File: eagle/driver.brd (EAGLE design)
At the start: 101.6 x 76.2 mm, 89 parts, among them IC1 XMEGA128A1, IC10 ST95P08M, IC11 ST95P08M, IC12 ST95P08M, IC13 ST95P08M, IC14 ST95P08M, IC15 ST95P08M, IC16 74AHC1G02DBV, IC17 74AHC1G02DBV, IC18 74AHC1G125DBV, IC19 74AHC1G125DBV, IC2 74AC16244, IC20 ST95P08M, IC21 ST95P08M, IC22 ST95P08M, IC23 ST95P08M, IC24 ST95P08M, IC25 ST95P08M, IC3 74AC16244, IC4 74AC16244, IC5 74AC16244, IC6 74AC16374, IC7 74AC16374, IC8 74AC16374, IC9 74AC16374

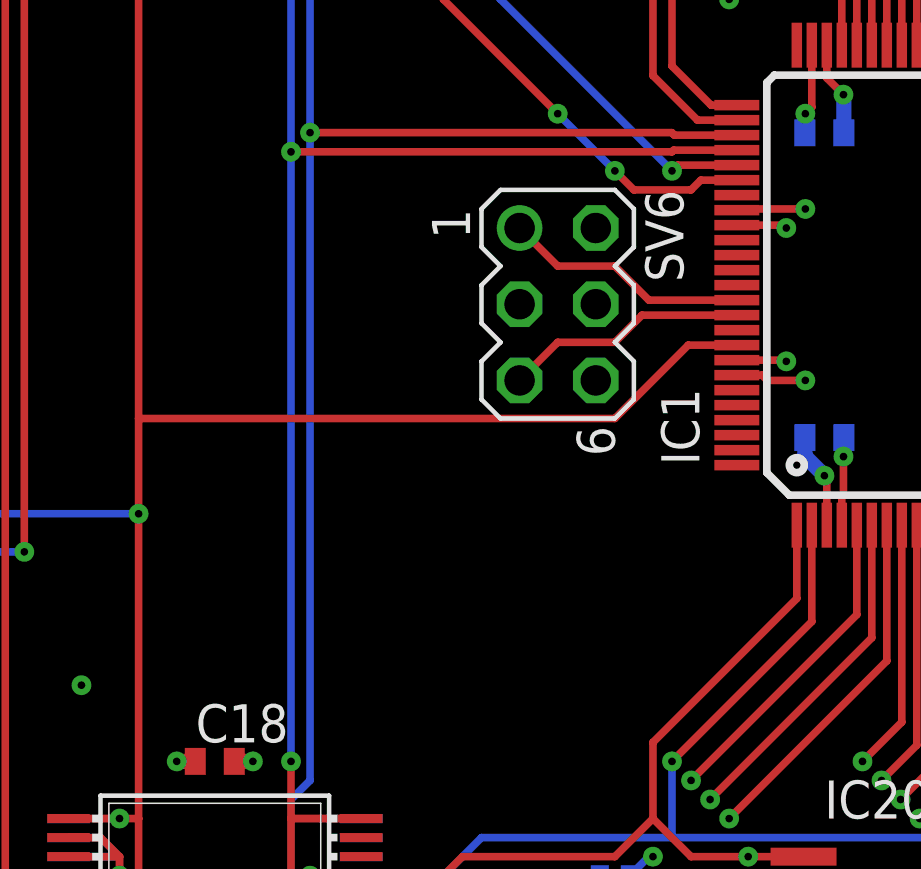
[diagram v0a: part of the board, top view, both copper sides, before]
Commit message: add reset button and status leds
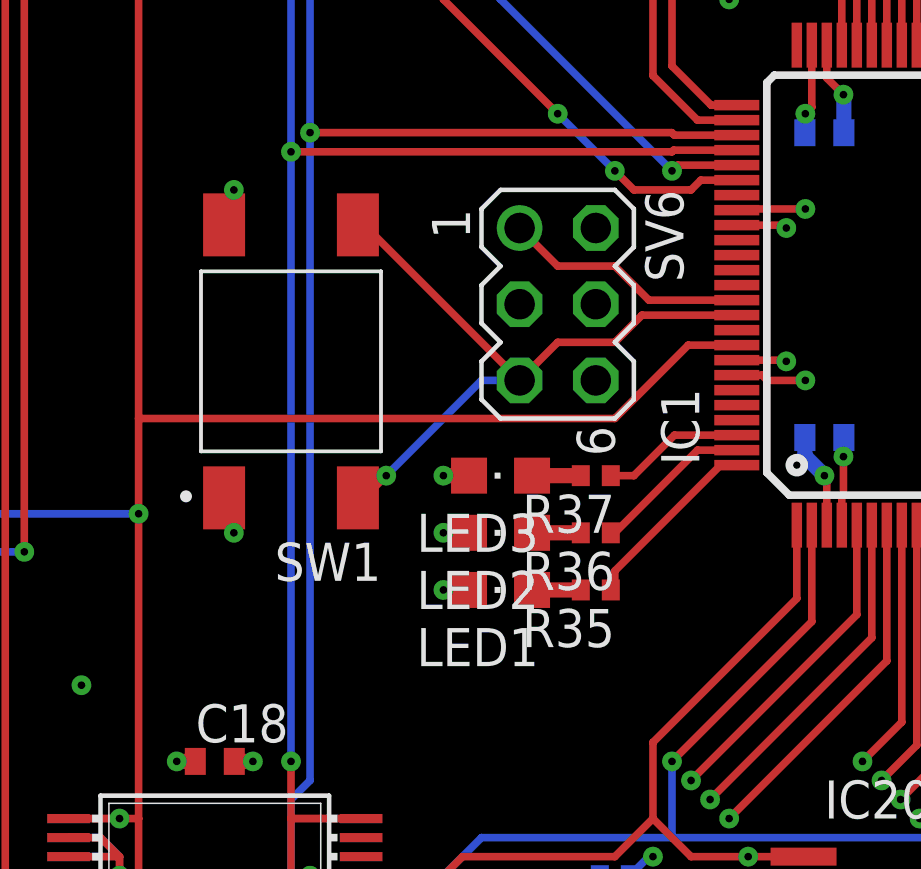
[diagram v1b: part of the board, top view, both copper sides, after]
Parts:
- added LED1, LED2, LED3: (no value), led:CHIPLED_0805
- added R35, R36, R37: 330, rcl:R0402
- added SW1: FSM2JSMA, Switch:FSM2JSMA
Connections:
- removed net N$88: IC1.90, SV6.5
- new net N$63: IC1.90, SV6.5, SW1.3, SW1.4
- new net N$66: LED3.A, R37.2
- new net N$67: LED2.A, R36.2
- new net N$69: LED1.A, R35.2
- new net N$71: IC1.100, R35.1
- new net N$73: IC1.99, R36.1
- new net N$75: IC1.98, R37.1
- net GND: now also LED1.C, LED2.C, LED3.C, SW1.1, SW1.2
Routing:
- net N$63: track 0.00 -> 22.7 mm, vias 0 -> 1
- net N$88: track 8.14 -> 0.00 mm
- net N$71: track 0.00 -> 6.22 mm
- net N$73: track 0.00 -> 5.34 mm
- net GND: track 187.5 -> 192.7 mm, vias 96 -> 101
- net N$75: track 0.00 -> 4.76 mm
- net N$69: track 0.00 -> 1.62 mm
- net N$67: track 0.00 -> 1.62 mm
- net N$66: track 0.00 -> 1.62 mm
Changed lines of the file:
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@@
 <layer number="132" name="bAdjust" color="7" fill="1" visible="yes" active="yes"/>
 <layer number="144" name="Drill_legend" color="7" fill="1" visible="yes" active="yes"/>
+<layer number="145" name="DrillLegend_01-16" color="2" fill="9" visible="no" active="yes"/>
+<layer number="146" name="DrillLegend_01-20" color="3" fill="9" visible="no" active="yes"/>
 <layer number="150" name="Notes" color="7" fill="1" visible="yes" active="yes"/>
 <layer number="151" name="HeatSink" color="7" fill="1" visible="yes" active="yes"/>
@@
 <attribute name="VALUE" x="36.195" y="13.335" size="1.27" layer="28" rot="MR0"/>
 </element>
+<element name="SW1" library="Switch" library_urn="urn:adsk.eagle:library:11396471" package="FSM2JSMA" package3d_urn="urn:adsk.eagle:package:12788212/3" value="FSM2JSMA" x="24.765" y="35.56" smashed="yes" rot="R180">
+<attribute name="CREATED_BY" value="PCBLayout.com" x="24.765" y="35.56" size="1.778" layer="27" rot="R180" display="off"/>
+<attribute name="DIGIKEY_PART_NUMBER" value="450-1130-ND" x="24.765" y="35.56" size="1.778" layer="27" rot="R180" display="off"/>
+<attribute name="MANUFACTURER" value="TE Connectivity ALCOSWITCH Switches" x="24.765" y="35.56" size="1.778" layer="27" rot="R180" display="off"/>
+<attribute name="MPN" value="FSM2JSMA" x="24.765" y="35.56" size="1.778" layer="27" rot="R180" display="off"/>
+<attribute name="NAME" x="27.76896875" y="29.51536875" size="1.27168125" layer="25" rot="R180"/>
+<attribute name="VALUE" x="28.01793125" y="42.85428125" size="1.27115" layer="27" rot="R180"/>
+</element>
+<element name="R35" library="rcl" library_urn="urn:adsk.eagle:library:334" package="R0402" package3d_urn="urn:adsk.eagle:package:23547/3" value="330" x="34.925" y="27.94" smashed="yes" rot="R180">
+<attribute name="NAME" x="35.56" y="27.305" size="1.27" layer="25" rot="R180"/>
+<attribute name="POPULARITY" value="34" x="34.925" y="27.94" size="1.778" layer="27" rot="R180" display="off"/>
+<attribute name="SPICEPREFIX" value="R" x="34.925" y="27.94" size="1.778" layer="27" rot="R180" display="off"/>
+<attribute name="VALUE" x="35.56" y="29.845" size="1.27" layer="27" rot="R180"/>
+</element>
+<element name="R36" library="rcl" library_urn="urn:adsk.eagle:library:334" package="R0402" package3d_urn="urn:adsk.eagle:package:23547/3" value="330" x="34.925" y="29.845" smashed="yes" rot="R180">
+<attribute name="NAME" x="35.56" y="29.21" size="1.27" layer="25" rot="R180"/>
+<attribute name="POPULARITY" value="34" x="34.925" y="29.845" size="1.778" layer="27" rot="R180" display="off"/>
+<attribute name="SPICEPREFIX" value="R" x="34.925" y="29.845" size="1.778" layer="27" rot="R180" display="off"/>
+<attribute name="VALUE" x="35.56" y="31.75" size="1.27" layer="27" rot="R180"/>
+</element>
+<element name="R37" library="rcl" library_urn="urn:adsk.eagle:library:334" package="R0402" package3d_urn="urn:adsk.eagle:package:23547/3" value="330" x="34.925" y="31.75" smashed="yes" rot="R180">
+<attribute name="NAME" x="35.56" y="31.115" size="1.27" layer="25" rot="R180"/>
+<attribute name="POPULARITY" value="34" x="34.925" y="31.75" size="1.778" layer="27" rot="R180" display="off"/>
+<attribute name="SPICEPREFIX" value="R" x="34.925" y="31.75" size="1.778" layer="27" rot="R180" display="off"/>
+<attribute name="VALUE" x="35.56" y="33.655" size="1.27" layer="27" rot="R180"/>
+</element>
+<element name="LED1" library="led" library_urn="urn:adsk.eagle:library:259" package="CHIPLED_0805" package3d_urn="urn:adsk.eagle:package:15821/2" value="" x="31.75" y="27.94" smashed="yes" rot="R90">
+<attribute name="NAME" x="33.02" y="26.67" size="1.27" layer="25" rot="R180"/>
+<attribute name="POPULARITY" value="52" x="31.75" y="27.94" size="1.778" layer="27" rot="R90" display="off"/>
+<attribute name="VALUE" x="33.02" y="30.48" size="1.27" layer="27" rot="R180"/>
+</element>
+<element name="LED2" library="led" library_urn="urn:adsk.eagle:library:259" package="CHIPLED_0805" package3d_urn="urn:adsk.eagle:package:15821/2" value="" x="31.75" y="29.845" smashed="yes" rot="R90">
+<attribute name="NAME" x="33.02" y="28.575" size="1.27" layer="25" rot="R180"/>
+<attribute name="POPULARITY" value="52" x="31.75" y="29.845" size="1.778" layer="27" rot="R90" display="off"/>
+<attribute name="VALUE" x="33.02" y="32.385" size="1.27" layer="27" rot="R180"/>
+</element>
+<element name="LED3" library="led" library_urn="urn:adsk.eagle:library:259" package="CHIPLED_0805" package3d_urn="urn:adsk.eagle:package:15821/2" value="" x="31.75" y="31.75" smashed="yes" rot="R90">
+<attribute name="NAME" x="33.02" y="30.48" size="1.27" layer="25" rot="R180"/>
+<attribute name="POPULARITY" value="52" x="31.75" y="31.75" size="1.778" layer="27" rot="R90" display="off"/>
+<attribute name="VALUE" x="33.02" y="34.29" size="1.27" layer="27" rot="R180"/>
+</element>
 </elements>
 <signals>
@@
 <wire x1="17.3482" y1="17.78" x2="18.415" y2="17.78" width="0.254" layer="16"/>
 <wire x1="18.415" y1="17.78" x2="19.05" y2="18.415" width="0.254" layer="16"/>
+<contactref element="SW1" pad="1"/>
+<contactref element="SW1" pad="2"/>
+<via x="22.86" y="41.275" extent="1-16" drill="0.254"/>
+<via x="22.86" y="29.845" extent="1-16" drill="0.254"/>
+<wire x1="22.535" y1="40.11" x2="22.535" y2="40.95" width="0.254" layer="1"/>
+<wire x1="22.535" y1="40.95" x2="22.86" y2="41.275" width="0.254" layer="1"/>
+<wire x1="22.535" y1="31.01" x2="22.86" y2="30.685" width="0.254" layer="1"/>
+<wire x1="22.86" y1="30.685" x2="22.86" y2="29.845" width="0.254" layer="1"/>
+<contactref element="LED1" pad="C"/>
+<contactref element="LED2" pad="C"/>
+<contactref element="LED3" pad="C"/>
+<via x="29.845" y="31.75" extent="1-16" drill="0.254"/>
+<via x="29.845" y="29.845" extent="1-16" drill="0.254"/>
+<via x="29.845" y="27.94" extent="1-16" drill="0.254"/>
+<wire x1="30.7" y1="31.75" x2="29.845" y2="31.75" width="0.508" layer="1"/>
+<wire x1="30.7" y1="29.845" x2="29.845" y2="29.845" width="0.508" layer="1"/>
+<wire x1="30.7" y1="27.94" x2="29.845" y2="27.94" width="0.508" layer="1"/>
 </signal>
 <signal name="VCC">
@@
 <wire x1="33.655" y1="38.735" x2="32.385" y2="40.005" width="0.254" layer="1"/>
 </signal>
-<signal name="N$88">
-<contactref element="IC1" pad="90"/>
-<contactref element="SV6" pad="5"/>
-<wire x1="39.625" y1="37.1" x2="36.465" y2="37.1" width="0.254" layer="1"/>
-<wire x1="36.465" y1="37.1" x2="35.56" y2="36.195" width="0.254" layer="1"/>
-<wire x1="35.56" y1="36.195" x2="33.655" y2="36.195" width="0.254" layer="1"/>
-<wire x1="33.655" y1="36.195" x2="32.385" y2="34.925" width="0.254" layer="1"/>
-</signal>
 <signal name="N$89">
 <contactref element="IC1" pad="38"/>
@@
 <wire x1="48.625" y1="23.765" x2="51.435" y2="20.955" width="0.254" layer="1"/>
 </signal>
+<signal name="N$63">
+<contactref element="SW1" pad="4"/>
+<contactref element="SW1" pad="3"/>
+<contactref element="IC1" pad="90"/>
+<contactref element="SV6" pad="5"/>
+<wire x1="39.625" y1="37.1" x2="36.465" y2="37.1" width="0.254" layer="1"/>
+<wire x1="36.465" y1="37.1" x2="35.56" y2="36.195" width="0.254" layer="1"/>
+<wire x1="35.56" y1="36.195" x2="33.655" y2="36.195" width="0.254" layer="1"/>
+<wire x1="33.655" y1="36.195" x2="32.385" y2="34.925" width="0.254" layer="1"/>
+<wire x1="32.385" y1="34.925" x2="27.2" y2="40.11" width="0.254" layer="1"/>
+<wire x1="27.2" y1="40.11" x2="26.995" y2="40.11" width="0.254" layer="1"/>
+<via x="27.94" y="31.75" extent="1-16" drill="0.254"/>
+<wire x1="27.94" y1="31.75" x2="27.2" y2="31.01" width="0.254" layer="1"/>
+<wire x1="27.2" y1="31.01" x2="26.995" y2="31.01" width="0.254" layer="1"/>
+<wire x1="27.94" y1="31.75" x2="31.115" y2="34.925" width="0.254" layer="16"/>
+<wire x1="31.115" y1="34.925" x2="32.385" y2="34.925" width="0.254" layer="16"/>
+</signal>
+<signal name="N$66">
+<contactref element="R37" pad="2"/>
+<contactref element="LED3" pad="A"/>
+<wire x1="32.8" y1="31.75" x2="34.425" y2="31.75" width="0.508" layer="1"/>
+</signal>
+<signal name="N$67">
+<contactref element="R36" pad="2"/>
+<contactref element="LED2" pad="A"/>
+<wire x1="32.8" y1="29.845" x2="34.425" y2="29.845" width="0.508" layer="1"/>
+</signal>
+<signal name="N$69">
+<contactref element="R35" pad="2"/>
+<contactref element="LED1" pad="A"/>
+<wire x1="32.8" y1="27.94" x2="34.425" y2="27.94" width="0.508" layer="1"/>
+</signal>
+<signal name="N$71">
+<contactref element="IC1" pad="100"/>
+<contactref element="R35" pad="1"/>
+<wire x1="35.425" y1="27.94" x2="35.56" y2="28.075" width="0.254" layer="1"/>
+<wire x1="35.56" y1="28.075" x2="35.56" y2="28.575" width="0.254" layer="1"/>
+<wire x1="39.085" y1="32.1" x2="39.625" y2="32.1" width="0.254" layer="1"/>
+<wire x1="35.56" y1="28.575" x2="39.085" y2="32.1" width="0.254" layer="1"/>
+</signal>
+<signal name="N$73">
+<contactref element="R36" pad="1"/>
+<contactref element="IC1" pad="99"/>
+<wire x1="35.425" y1="29.845" x2="35.56" y2="29.845" width="0.254" layer="1"/>
+<wire x1="38.315" y1="32.6" x2="39.625" y2="32.6" width="0.254" layer="1"/>
+<wire x1="35.56" y1="29.845" x2="38.315" y2="32.6" width="0.254" layer="1"/>
+</signal>
+<signal name="N$75">
+<contactref element="IC1" pad="98"/>
+<contactref element="R37" pad="1"/>
+<wire x1="35.425" y1="31.75" x2="36.195" y2="31.75" width="0.254" layer="1"/>
+<wire x1="37.545" y1="33.1" x2="39.625" y2="33.1" width="0.254" layer="1"/>
+<wire x1="36.195" y1="31.75" x2="37.545" y2="33.1" width="0.254" layer="1"/>
+</signal>
 </signals>

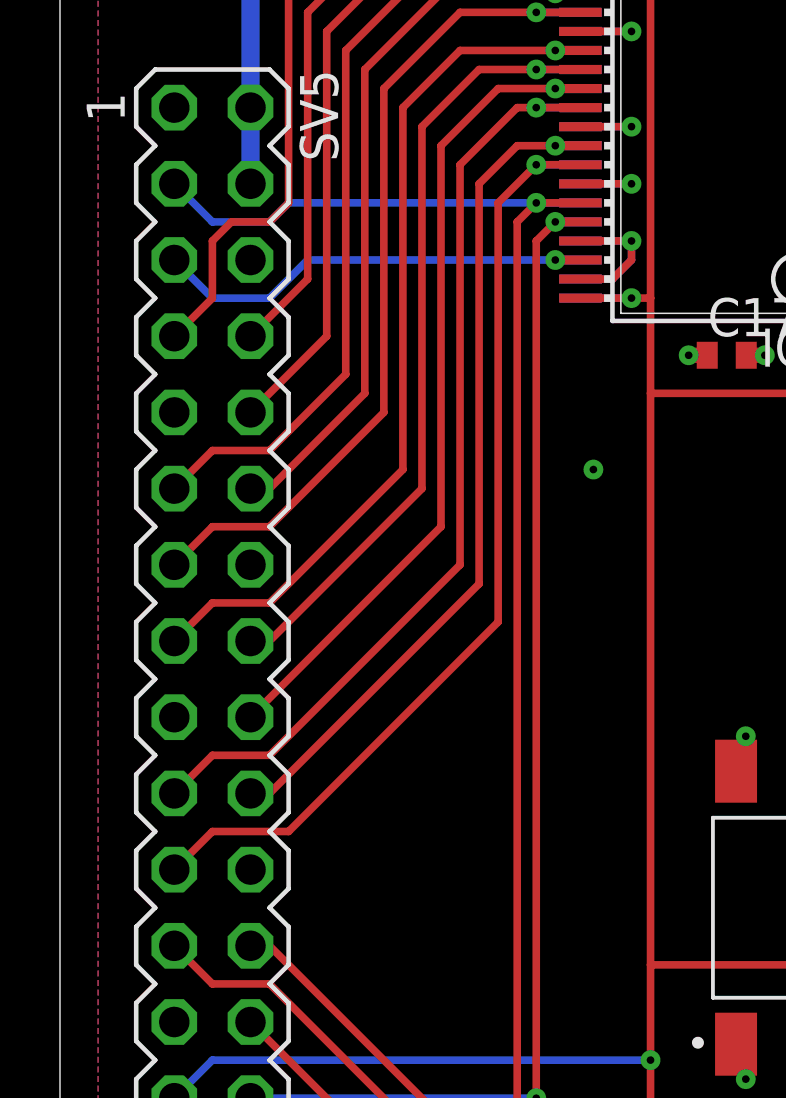
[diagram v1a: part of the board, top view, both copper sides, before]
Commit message: fix pinout for rpi header
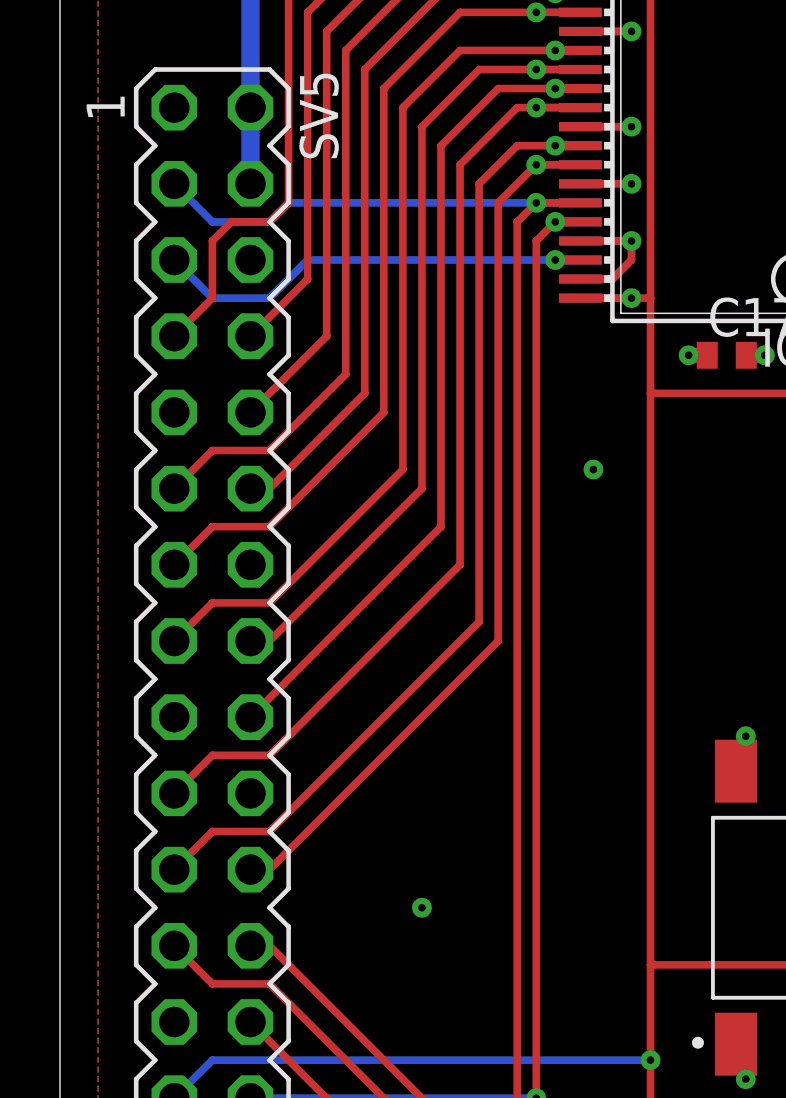
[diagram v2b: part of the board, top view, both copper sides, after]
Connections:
- net GND: now also SV5.20; no longer SV5.22
- net N$30: now also SV5.22; no longer SV5.21
- net N$34: now also SV5.21; no longer SV5.20
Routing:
- net N$34: track 28.6 -> 32.9 mm
- net N$30: track 32.9 -> 30.8 mm
- net GND: vias 101 -> 102
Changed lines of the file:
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@@
 <contactref element="SV5" pad="6"/>
 <contactref element="SV5" pad="14"/>
-<contactref element="SV5" pad="22"/>
 <contactref element="SV5" pad="25"/>
 <contactref element="SV5" pad="39"/>
@@
 <wire x1="30.7" y1="29.845" x2="29.845" y2="29.845" width="0.508" layer="1"/>
 <wire x1="30.7" y1="27.94" x2="29.845" y2="27.94" width="0.508" layer="1"/>
+<contactref element="SV5" pad="20"/>
+<via x="12.065" y="35.56" extent="1-16" drill="0.254"/>
 </signal>
 <signal name="VCC">
@@
 <contactref element="IC6" pad="32"/>
 <contactref element="IC7" pad="41"/>
-<contactref element="SV5" pad="21"/>
-<wire x1="3.81" y1="36.83" x2="5.08" y2="38.1" width="0.254" layer="1"/>
-<wire x1="5.08" y1="38.1" x2="7.62" y2="38.1" width="0.254" layer="1"/>
-<wire x1="7.62" y1="38.1" x2="14.605" y2="45.085" width="0.254" layer="1"/>
-<wire x1="14.605" y1="45.085" x2="14.605" y2="59.055" width="0.254" layer="1"/>
+<wire x1="14.605" y1="44.45" x2="14.605" y2="59.055" width="0.254" layer="1"/>
 <wire x1="14.605" y1="59.055" x2="15.875" y2="60.325" width="0.254" layer="1"/>
 <wire x1="15.875" y1="60.325" x2="17.3482" y2="60.325" width="0.254" layer="1"/>
 <via x="15.875" y="60.325" extent="1-16" drill="0.254"/>
 <wire x1="17.3482" y1="60.325" x2="15.875" y2="60.325" width="0.254" layer="16"/>
+<contactref element="SV5" pad="22"/>
+<wire x1="6.35" y1="36.83" x2="6.985" y2="36.83" width="0.254" layer="1"/>
+<wire x1="14.605" y1="44.45" x2="6.985" y2="36.83" width="0.254" layer="1"/>
 </signal>
 <signal name="N$34">
 <contactref element="IC7" pad="40"/>
 <contactref element="IC6" pad="33"/>
-<contactref element="SV5" pad="20"/>
-<wire x1="6.35" y1="39.37" x2="6.985" y2="39.37" width="0.254" layer="1"/>
-<wire x1="6.985" y1="39.37" x2="13.97" y2="46.355" width="0.254" layer="1"/>
+<wire x1="13.97" y1="45.085" x2="6.985" y2="38.1" width="0.254" layer="1"/>
 <wire x1="13.97" y1="59.69" x2="15.24" y2="60.96" width="0.254" layer="1"/>
 <wire x1="15.24" y1="60.96" x2="16.51" y2="60.96" width="0.254" layer="1"/>
 <wire x1="16.51" y1="60.96" x2="17.3482" y2="60.96" width="0.254" layer="1"/>
-<wire x1="13.97" y1="46.355" x2="13.97" y2="59.69" width="0.254" layer="1"/>
+<wire x1="13.97" y1="45.085" x2="13.97" y2="59.69" width="0.254" layer="1"/>
 <via x="16.51" y="60.96" extent="1-16" drill="0.254"/>
 <wire x1="17.3482" y1="60.96" x2="16.51" y2="60.96" width="0.254" layer="16"/>
+<contactref element="SV5" pad="21"/>
+<wire x1="6.985" y1="38.1" x2="5.08" y2="38.1" width="0.254" layer="1"/>
+<wire x1="5.08" y1="38.1" x2="3.81" y2="36.83" width="0.254" layer="1"/>
 </signal>
 <signal name="N$40">
